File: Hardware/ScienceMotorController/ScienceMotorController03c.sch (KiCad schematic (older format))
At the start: 17 parts, among them U4 VNH5019A_E

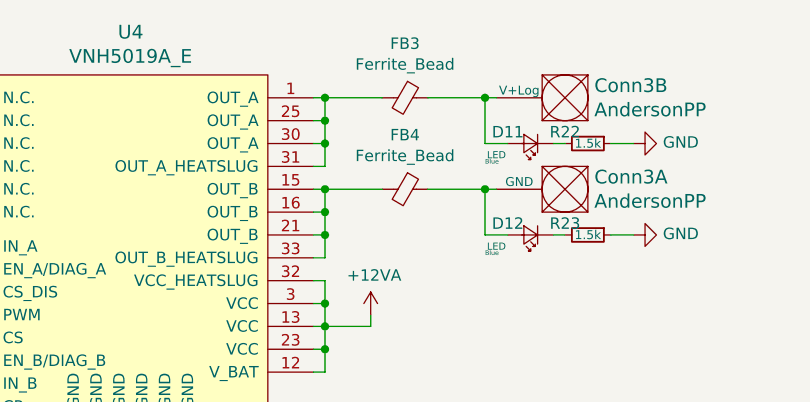
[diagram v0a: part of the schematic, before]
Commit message: finished assigning footprints, generated pcbnew
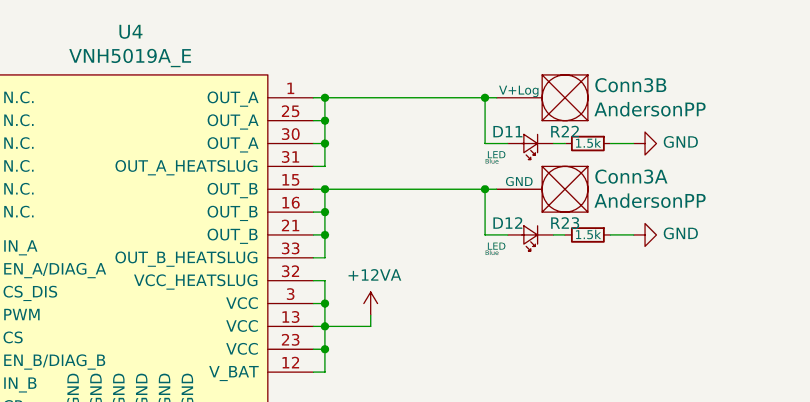
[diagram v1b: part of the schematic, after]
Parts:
- removed FB3, FB4: Ferrite_Bead, symbol Device:Ferrite_Bead_Small
- Conn3: footprint MRDT_Connectors:Anderson_2_Vertical_Sidy_by_Side -> MRDT_Connectors:Anderson_2_Horizontal_Side_by_Side
- U4: footprint (none) -> MRDT_ICs:MultiPowerSO_30
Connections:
- net at Conn3.2 (V+Log), D11.2 (A): now also U4.1 (OUT_A), U4.25 (OUT_A), U4.30 (OUT_A), U4.31 (OUT_A_HEATSLUG)
- net at Conn3.1 (GND), D12.2 (A): now also U4.15 (OUT_B), U4.16 (OUT_B), U4.21 (OUT_B), U4.33 (OUT_B_HEATSLUG)
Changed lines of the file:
@@
 F 0 "U4" H 6100 6137 60  0000 C CNN
 F 1 "VNH5019A_E" H 6100 6031 60  0000 C CNN
-F 2 "" H 5500 5750 60  0001 C CNN
+F 2 "MRDT_ICs:MultiPowerSO_30" H 5500 5750 60  0001 C CNN
 F 3 "" H 5500 5750 60  0001 C CNN
 	1    5500 4450
@@
 F 0 "Conn3" H 8072 3397 60  0000 R CNN
 F 1 "AndersonPP" H 8072 3503 60  0000 R CNN
-F 2 "MRDT_Connectors:Anderson_2_Vertical_Sidy_by_Side" H 7950 2800 60  0001 C CNN
+F 2 "MRDT_Connectors:Anderson_2_Horizontal_Side_by_Side" H 7950 2800 60  0001 C CNN
 F 3 "" H 7950 2800 60  0001 C CNN
 	1    8100 3350
@@
 F 0 "Conn3" H 8072 2997 60  0000 R CNN
 F 1 "AndersonPP" H 8072 3103 60  0000 R CNN
-F 2 "MRDT_Connectors:Anderson_2_Vertical_Sidy_by_Side" H 7950 2400 60  0001 C CNN
+F 2 "MRDT_Connectors:Anderson_2_Horizontal_Side_by_Side" H 7950 2400 60  0001 C CNN
 F 3 "" H 7950 2400 60  0001 C CNN
 	2    8100 2950
@@
 	5300 4100 4350 4100
 Connection ~ 4350 4100
-Wire Wire Line
-	7400 3050 7650 3050
-Wire Wire Line
-	7400 3450 7650 3450
 Wire Wire Line
 	7650 3250 7650 3050
@@
 	1    0    0    -1
 $EndComp
-$Comp
-L Device:Ferrite_Bead_Small FB?
-U 1 1 5F9DB37B
-P 7300 3050
-AR Path="/5F9082FA/5F9DB37B" Ref="FB?"  Part="1"
-AR Path="/5F7148FA/5FA34AD7/5F9DB37B" Ref="FB3"  Part="1"
-F 0 "FB3" V 7063 3050 50  0000 C CNN
-F 1 "Ferrite_Bead" V 7154 3050 50  0000 C CNN
-F 2 "" V 7230 3050 50  0001 C CNN
-F 3 "~" H 7300 3050 50  0001 C CNN
-	1    7300 3050
-	0    1    1    0
-$EndComp
-$Comp
-L Device:Ferrite_Bead_Small FB?
-U 1 1 5F9DBDAC
-P 7300 3450
-AR Path="/5F9082FA/5F9DBDAC" Ref="FB?"  Part="1"
-AR Path="/5F7148FA/5FA34AD7/5F9DBDAC" Ref="FB4"  Part="1"
-F 0 "FB4" V 7063 3450 50  0000 C CNN
-F 1 "Ferrite_Bead" V 7154 3450 50  0000 C CNN
-F 2 "" V 7230 3450 50  0001 C CNN
-F 3 "~" H 7300 3450 50  0001 C CNN
-	1    7300 3450
-	0    1    1    0
-$EndComp
-Wire Wire Line
-	6950 3050 7200 3050
 Connection ~ 6950 3050
-Wire Wire Line
-	7200 3450 6950 3450
 Connection ~ 6950 3450
 Text HLabel 4850 3700 0    50   Input ~ 0
@@
 Text Notes 7650 3750 0    20   ~ 0
 Blue
+Wire Wire Line
+	6950 3450 7650 3450
+Wire Wire Line
+	6950 3050 7650 3050
 $EndSCHEMATC

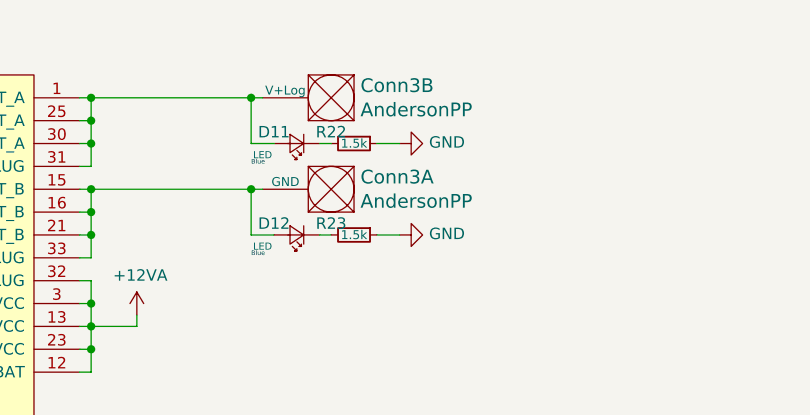
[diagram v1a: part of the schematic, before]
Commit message: running traces
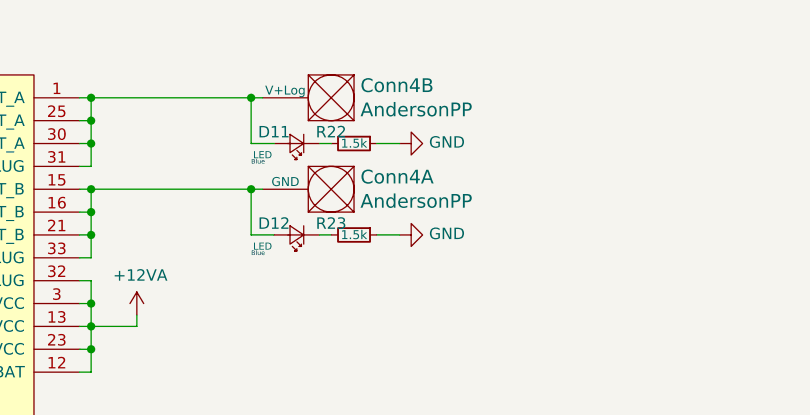
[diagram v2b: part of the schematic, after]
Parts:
- renumbered Conn3 to Conn4
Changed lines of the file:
@@
 AR Path="/5F7D111E/5FA660A7/5FA7B86E" Ref="Conn?"  Part="1"
 AR Path="/5F9082FA/5FA7B86E" Ref="Conn?"  Part="1"
-AR Path="/5F7148FA/5FA34AD7/5FA7B86E" Ref="Conn3"  Part="1"
-F 0 "Conn3" H 8072 3397 60  0000 R CNN
+AR Path="/5F7148FA/5FA34AD7/5FA7B86E" Ref="Conn4"  Part="1"
+F 0 "Conn4" H 8072 3397 60  0000 R CNN
 F 1 "AndersonPP" H 8072 3503 60  0000 R CNN
 F 2 "MRDT_Connectors:Anderson_2_Horizontal_Side_by_Side" H 7950 2800 60  0001 C CNN
@@
 AR Path="/5F7D111E/5FA660A7/5FA7B874" Ref="Conn?"  Part="2"
 AR Path="/5F9082FA/5FA7B874" Ref="Conn?"  Part="2"
-AR Path="/5F7148FA/5FA34AD7/5FA7B874" Ref="Conn3"  Part="2"
-F 0 "Conn3" H 8072 2997 60  0000 R CNN
+AR Path="/5F7148FA/5FA34AD7/5FA7B874" Ref="Conn4"  Part="2"
+F 0 "Conn4" H 8072 2997 60  0000 R CNN
 F 1 "AndersonPP" H 8072 3103 60  0000 R CNN
 F 2 "MRDT_Connectors:Anderson_2_Horizontal_Side_by_Side" H 7950 2400 60  0001 C CNN
